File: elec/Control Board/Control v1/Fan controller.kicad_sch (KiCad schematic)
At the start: 35 parts, among them J10 Conn_01x05, J11 Conn_01x04, J12 Conn_01x07, J18 Conn_01x04_Pin, J6 DB25_Female_MountingHoles, J9 Conn_01x04, Q2 NCE01P30K, Q601 BSS138

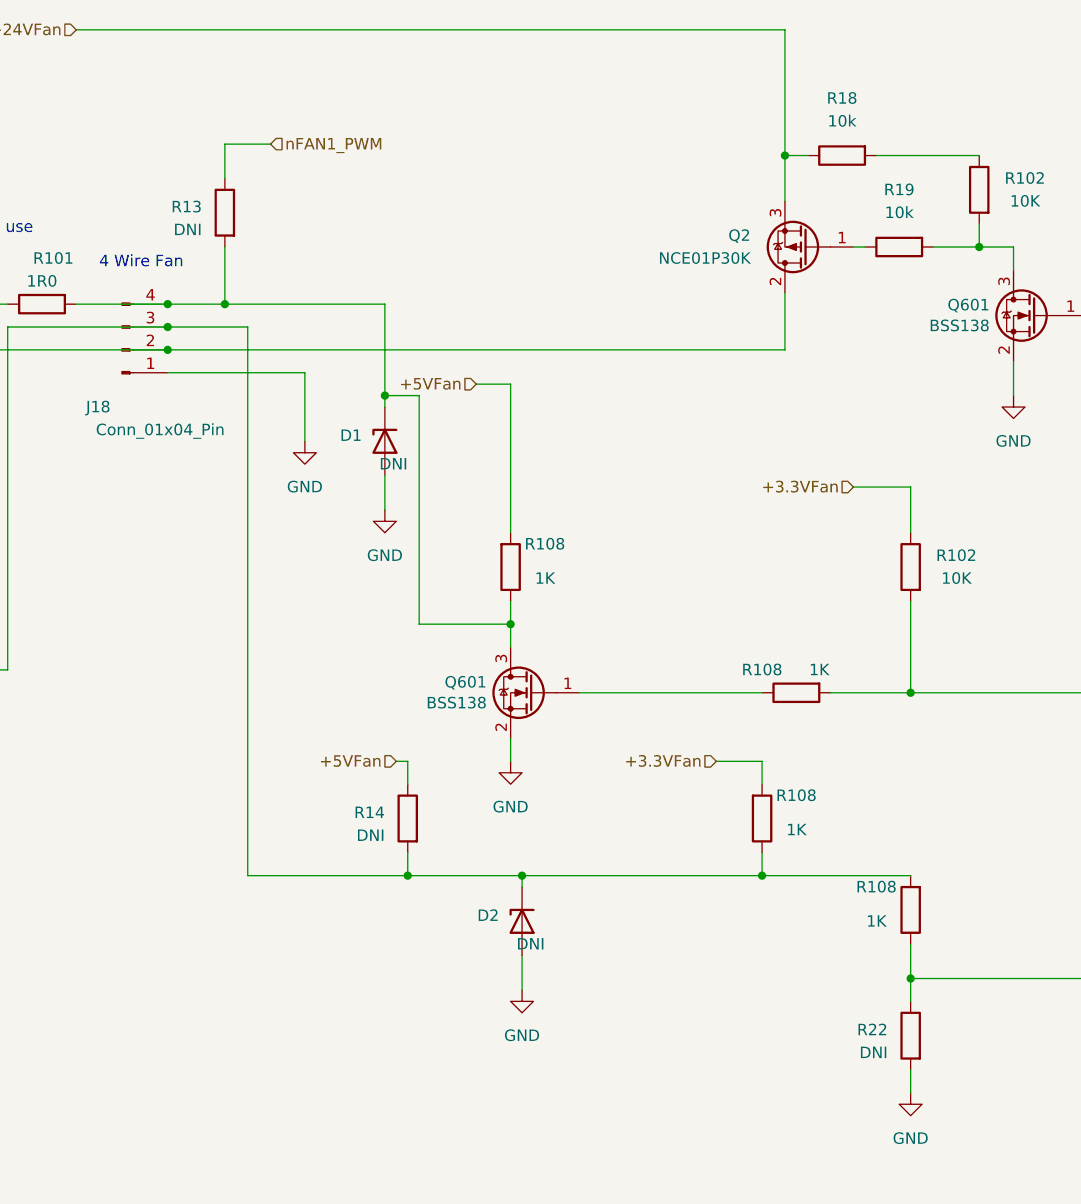
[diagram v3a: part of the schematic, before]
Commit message: More update schematic for MCP9600 I2C thermocouple.
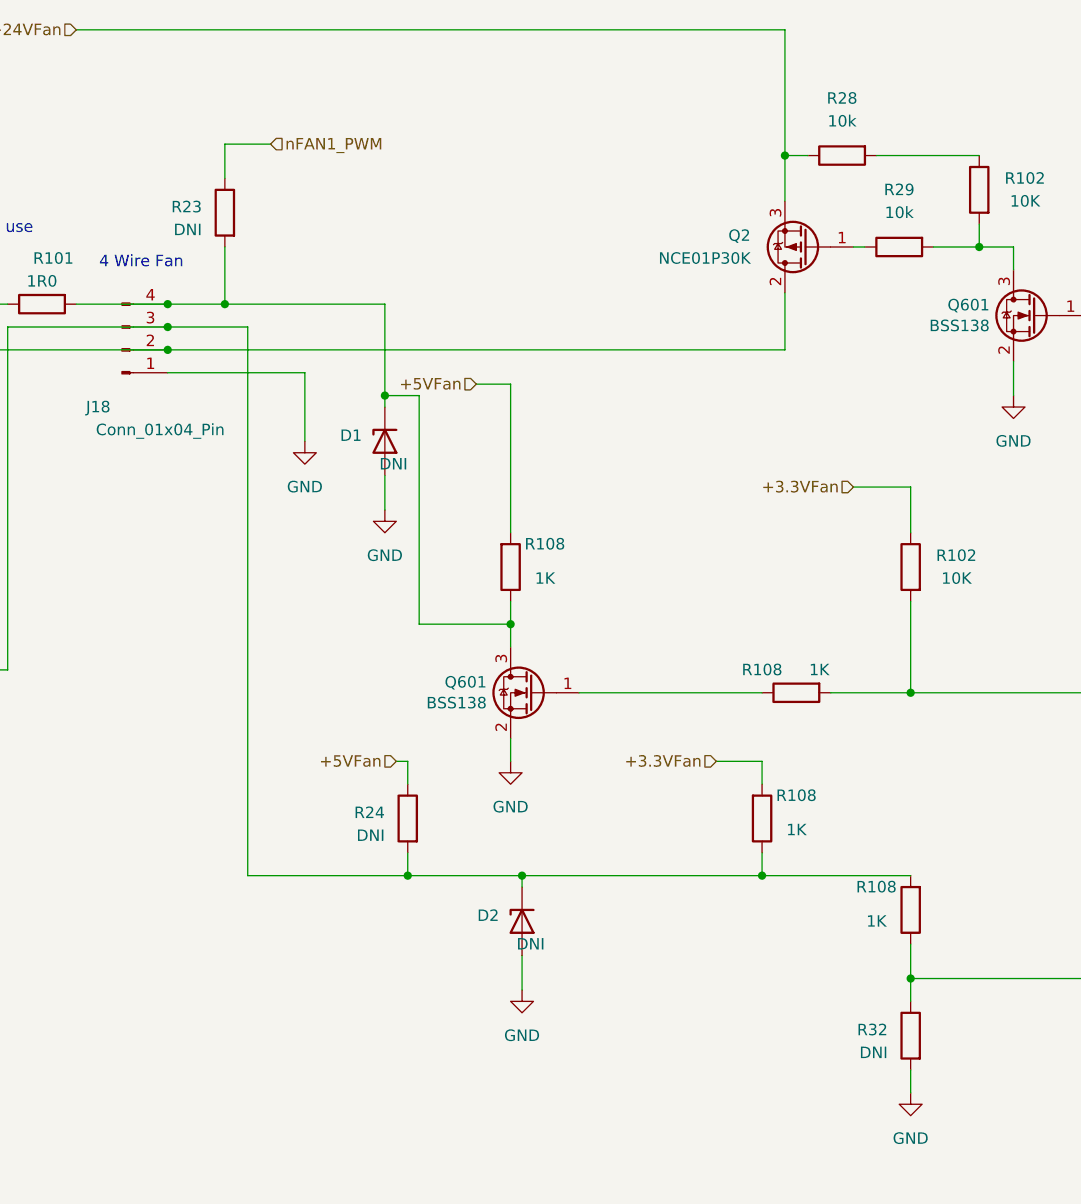
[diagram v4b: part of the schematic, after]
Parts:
- renumbered R13 to R23, R14 to R24, R18 to R28, R19 to R29, R22 to R32

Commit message: Fix swome ERC errors.
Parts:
- R32: renamed from R24; footprint (none) -> Resistor_SMD:R_0603_1608Metric_Pad0.98x0.95mm_HandSolder
- R40: renamed from R32; footprint (none) -> Resistor_SMD:R_0603_1608Metric_Pad0.98x0.95mm_HandSolder
- renumbered J18 to J20, R23 to R31, R28 to R36, R29 to R37

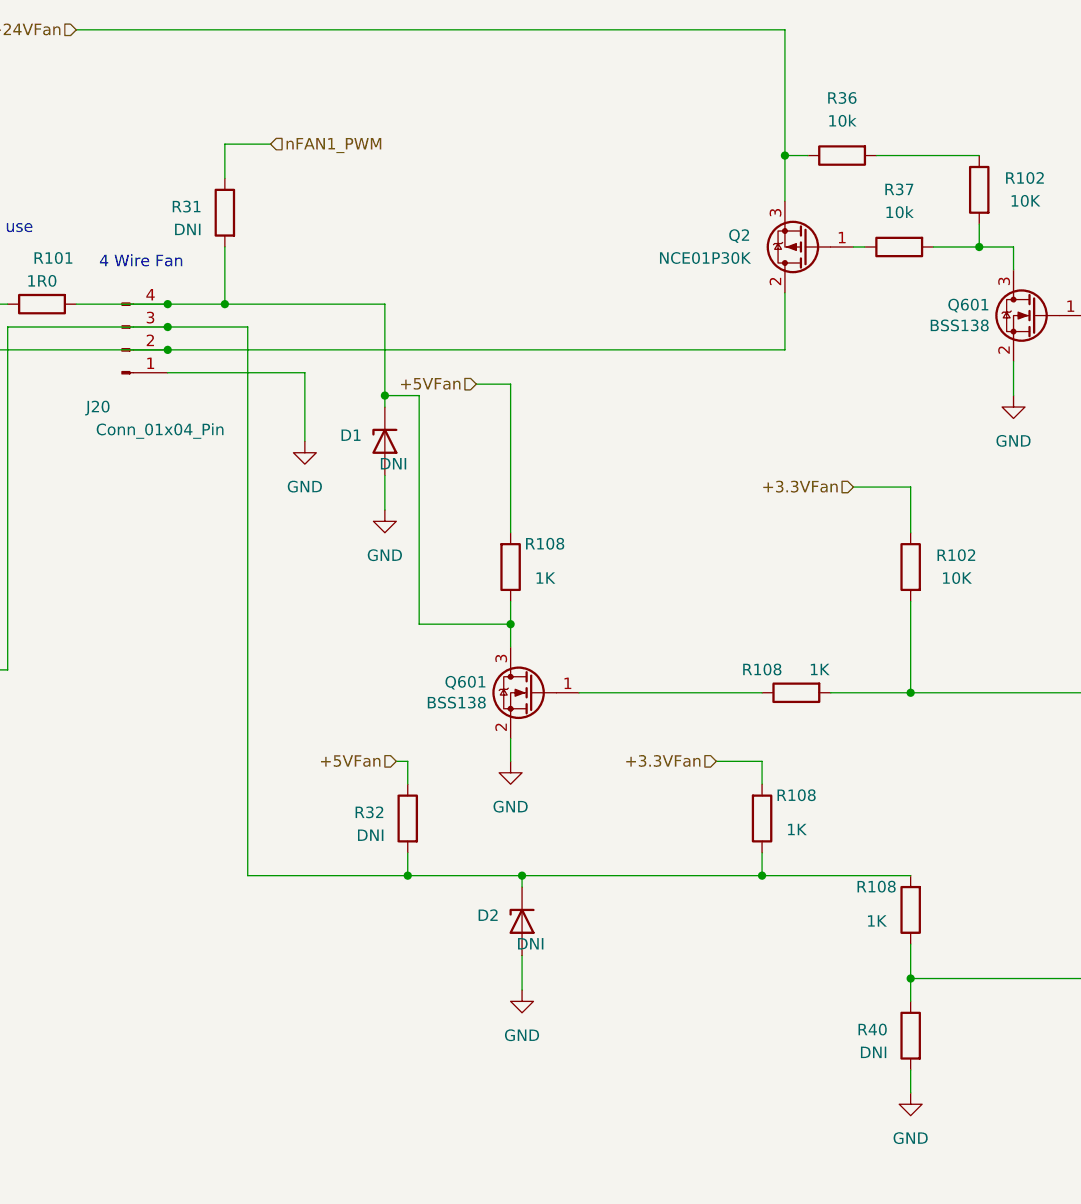
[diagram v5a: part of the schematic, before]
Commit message: Place PCB components.
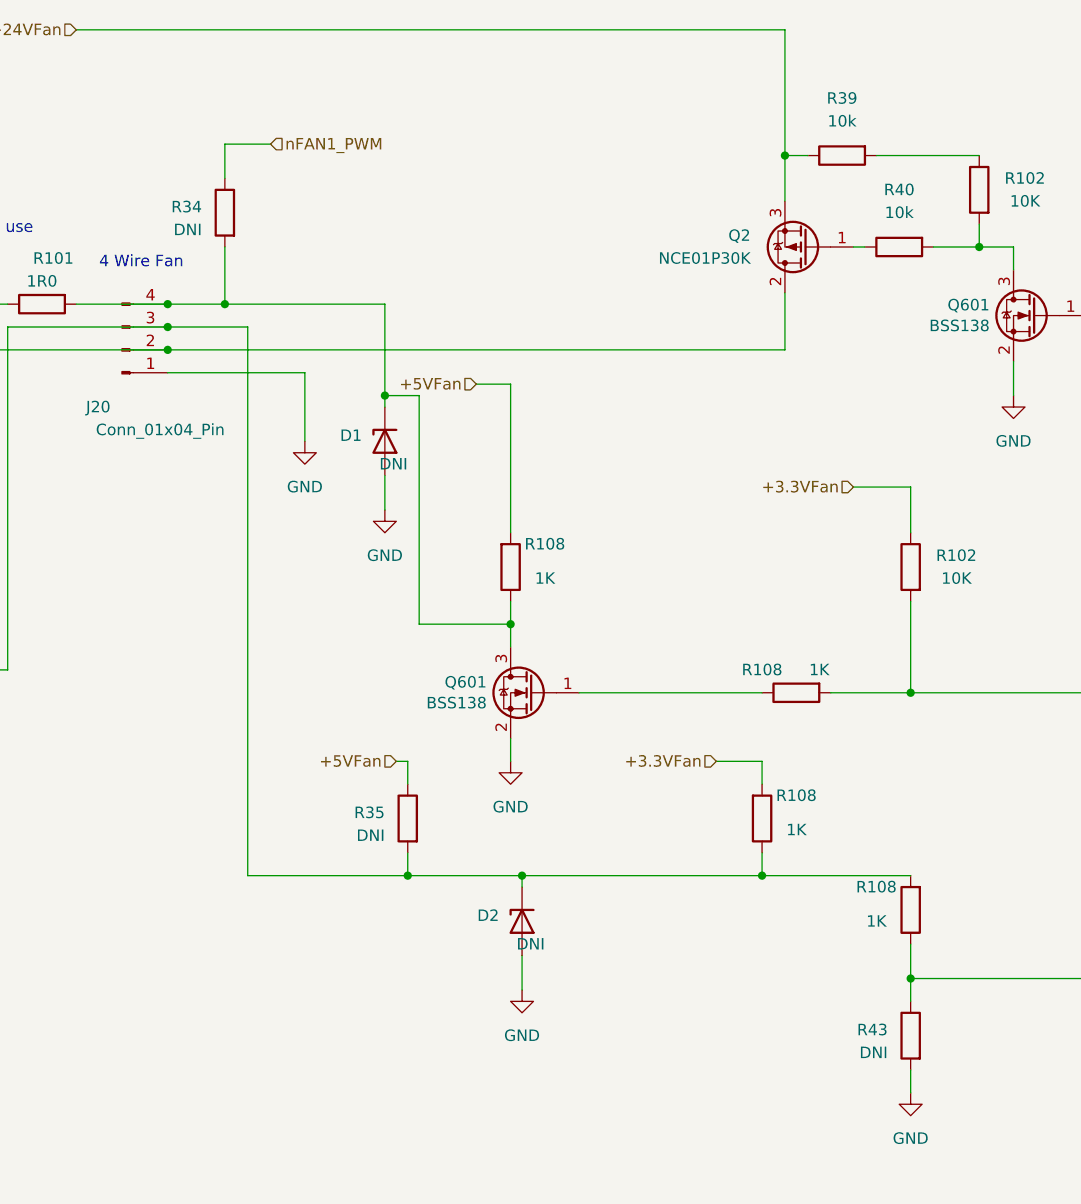
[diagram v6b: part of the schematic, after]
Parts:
- renumbered R31 to R34, R32 to R35, R36 to R39, R37 to R40, R40 to R43

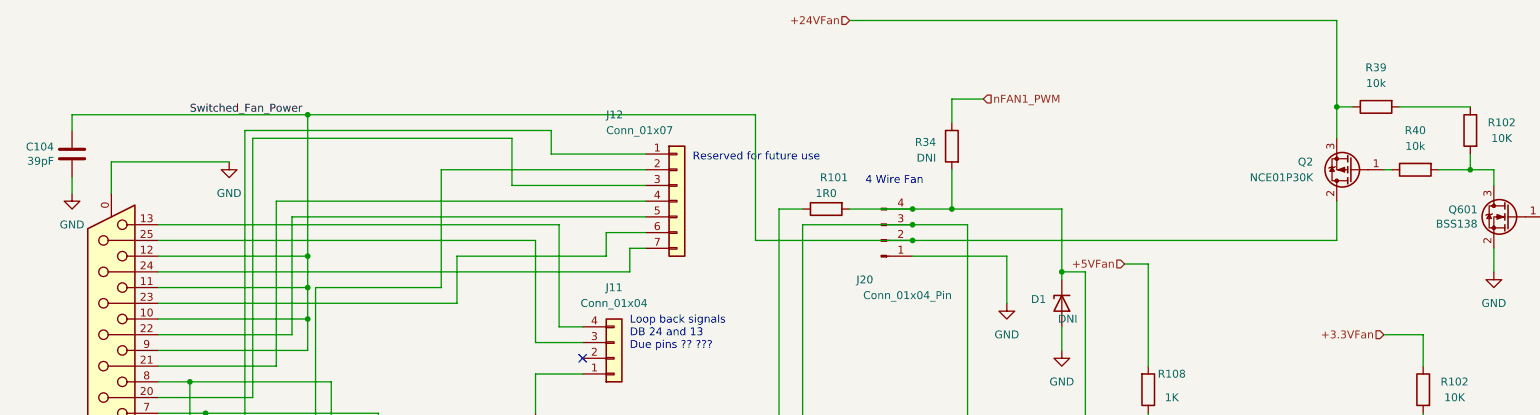
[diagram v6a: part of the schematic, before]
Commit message: Net name congruancy.
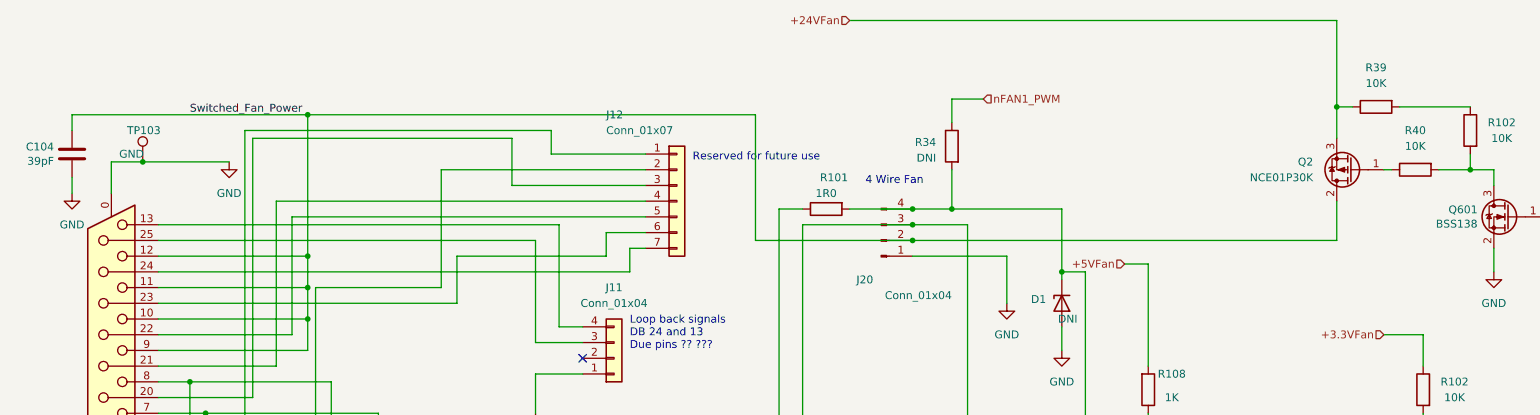
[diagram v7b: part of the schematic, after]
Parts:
- added TP103: GND, TestPoint:TestPoint_Loop_D2.54mm_Drill1.5mm_Beaded, symbol Connector:TestPoint
- J10, J11, J12, J9: AssemblyType (none) -> HAND
- J20: value Conn_01x04_Pin -> Conn_01x04; AssemblyType (none) -> HAND
- R102: LongLead (none) -> NO
- R39, R40: value 10k -> 10K; footprint (none) -> Resistor_SMD:R_0603_1608Metric_Pad0.98x0.95mm_HandSolder; AssemblyType (none) -> SMT; Cost (none) -> 0.0015; Distributor 1 (none) -> JLCPCB; Distributor 1 PN (none) -> C269701
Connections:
- net GND: now also TP103.1

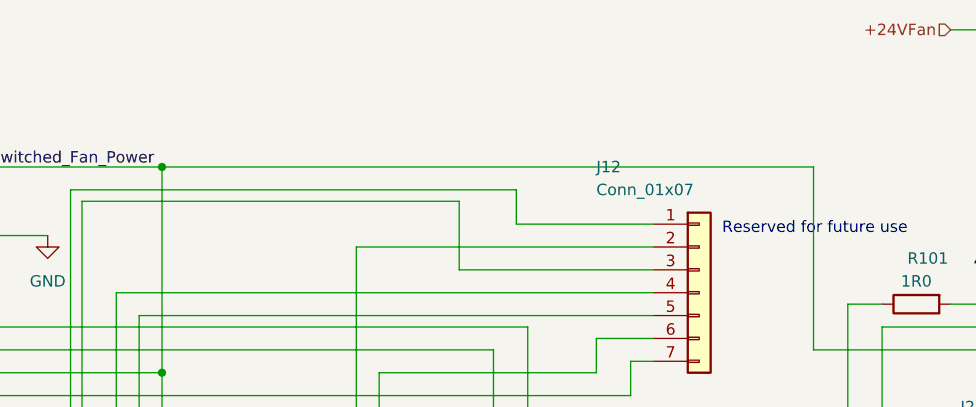
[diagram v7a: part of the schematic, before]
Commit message: Net name congruancy to D35. Add named test points.
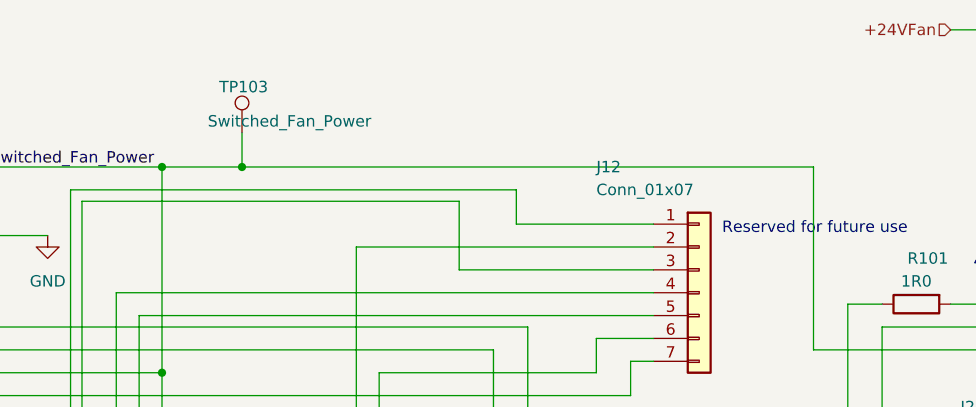
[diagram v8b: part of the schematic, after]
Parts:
- added TP103: Switched_Fan_Power, TestPoint:TestPoint_Loop_D2.54mm_Drill1.5mm_Beaded, symbol Connector:TestPoint
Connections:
- net Switched_Fan_Power: now also TP103.1
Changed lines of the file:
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@@
   (junction (at 199.39 96.52) (diameter 0) (color 0 0 0 0)
   )
+  (junction (at 72.39 45.72) (diameter 0) (color 0 0 0 0)
+  )
   (junction (at 62.23 144.78) (diameter 0) (color 0 0 0 0)
   )
@@
     (stroke (width 0) (type default))
   )
+  (wire (pts (xy 72.39 45.72) (xy 135.89 45.72))
+    (stroke (width 0) (type default))
+  )
   (wire (pts (xy 49.53 99.06) (xy 81.28 99.06))
     (stroke (width 0) (type default))
@@
     (stroke (width 0) (type default))
   )
-  (wire (pts (xy 63.5 45.72) (xy 135.89 45.72))
+  (wire (pts (xy 63.5 45.72) (xy 72.39 45.72))
     (stroke (width 0) (type default))
   )
@@
     (stroke (width 0) (type default))
   )
+  (wire (pts (xy 72.39 41.91) (xy 72.39 45.72))
+    (stroke (width 0) (type default))
+  )
   (wire (pts (xy 39.37 124.46) (xy 54.61 124.46))
     (stroke (width 0) (type default))
@@
     )
   )
+  (symbol (lib_id "Connector:TestPoint") (at 72.39 41.91 0) (unit 1)
+    (in_bom yes) (on_board yes) (dnp no)
+    (property "Reference" "TP103" (at 69.85 36.83 0)
+      (effects (font (size 1.27 1.27)) (justify left))
+    )
+    (property "Value" "Switched_Fan_Power" (at 68.58 40.64 0)
+      (effects (font (size 1.27 1.27)) (justify left))
+    )
+    (property "Footprint" "TestPoint:TestPoint_Loop_D2.54mm_Drill1.5mm_Beaded" (at 77.47 41.91 0)
+      (effects (font (size 1.27 1.27)) hide)
+    )
+    (property "Datasheet" "~" (at 77.47 41.91 0)
+      (effects (font (size 1.27 1.27)) hide)
+    )
+    (property "AssemblyType" "HAND" (at 72.39 41.91 0)
+      (effects (font (size 1.27 1.27)) hide)
+    )
+    (pin "1")
+    (instances
+      (project "GeneralPurposeAlarmDevicePCB"
+        (path "/412a327d-1ee3-473e-bc00-1545004b7edf"
+          (reference "TP103") (unit 1)
+        )
+      )
+      (project "Control v1"
+        (path "/c68c9deb-8d4d-42f0-adf8-4d3022f4ee59/3ff32a52-b1ed-4756-8661-90a95f721605"
+          (reference "TP1") (unit 1)
+        )
+        (path "/c68c9deb-8d4d-42f0-adf8-4d3022f4ee59"
+          (reference "TP1") (unit 1)
+        )
+        (path "/c68c9deb-8d4d-42f0-adf8-4d3022f4ee59/0cb2f0dc-fe38-451d-b752-5d12a98f8d03"
+          (reference "TPSwitched_Fan_Power1") (unit 1)
+        )
+      )
+    )
+  )
   (symbol (lib_id "Device:C") (at 81.28 133.35 0) (mirror y) (unit 1)
     (in_bom yes) (on_board yes) (dnp no)
@@
         )
         (path "/c68c9deb-8d4d-42f0-adf8-4d3022f4ee59/0cb2f0dc-fe38-451d-b752-5d12a98f8d03"
-          (reference "TP13") (unit 1)
+          (reference "TP11") (unit 1)
         )
       )
